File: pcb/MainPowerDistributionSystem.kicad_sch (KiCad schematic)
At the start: 6 parts, among them J2 PREC040DBAN-M71RC, U1 TPS22810DRV, U2 D24V7F5, U3 D24V7F3

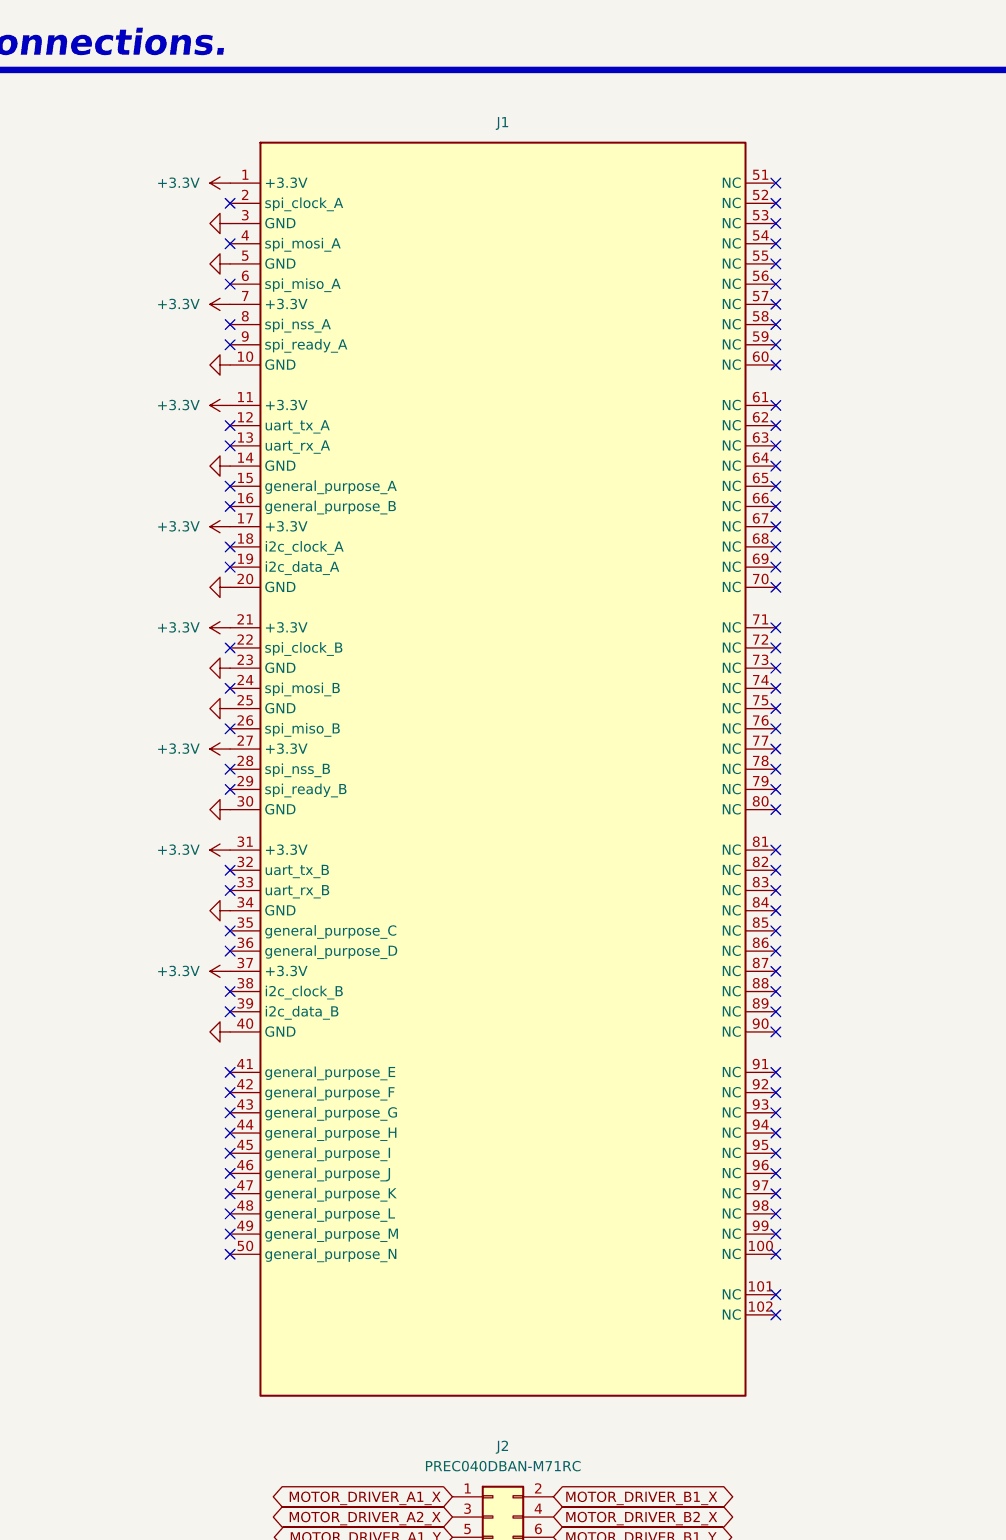
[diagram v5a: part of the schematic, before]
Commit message: Updated main stack-up connector design to go from 6 1x17 headers to only 4 1x17 headers.
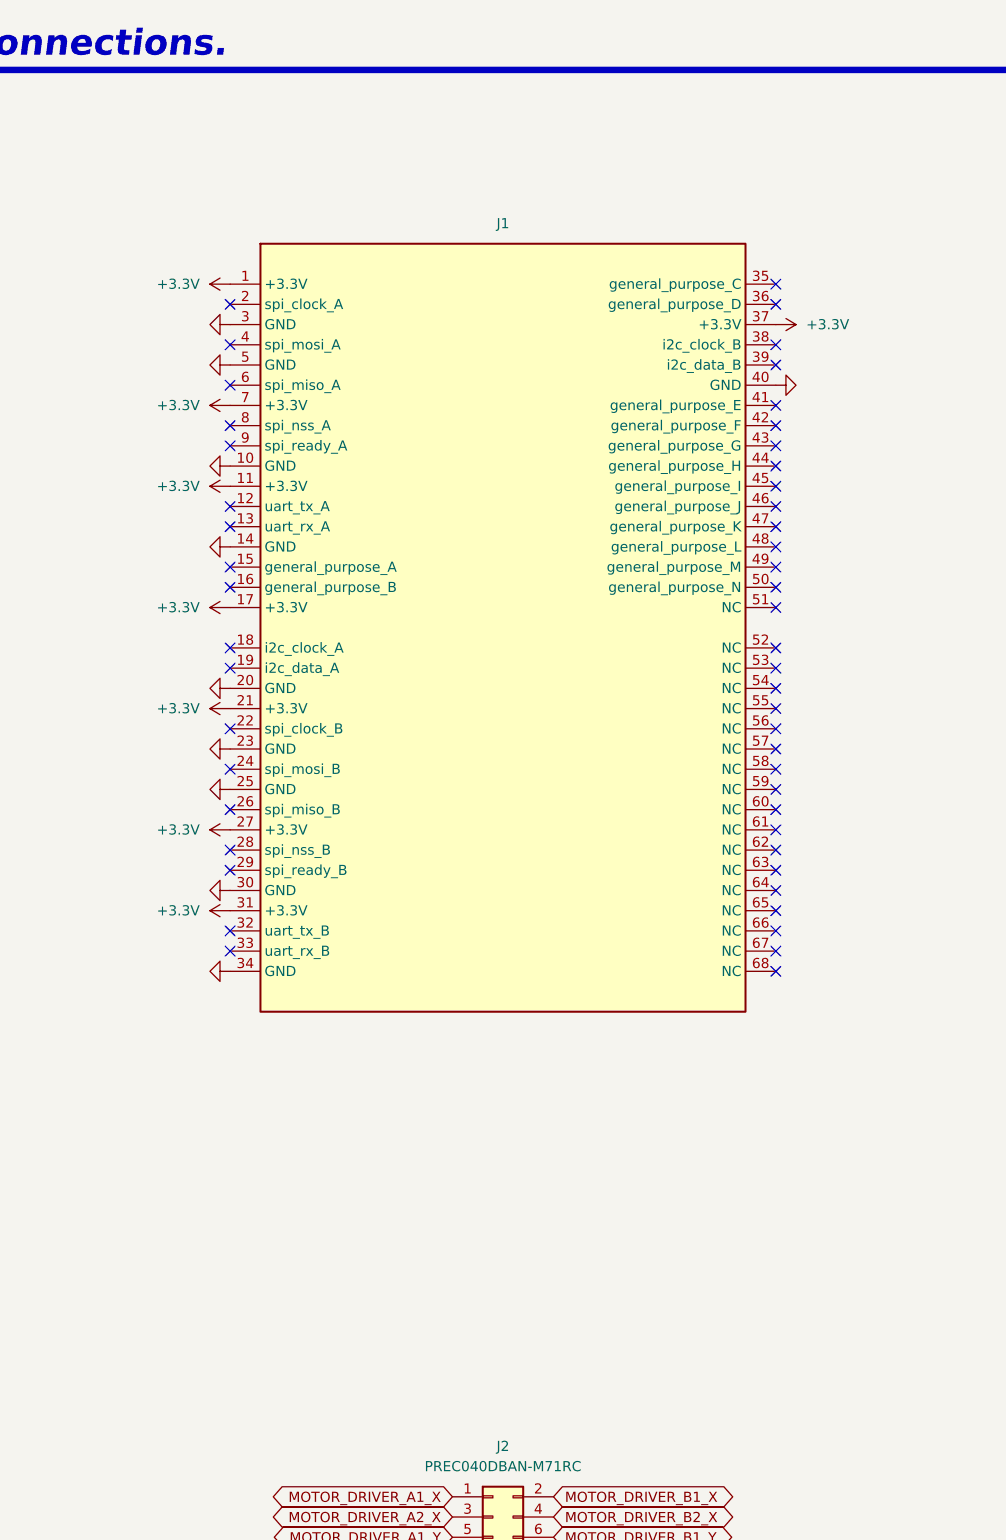
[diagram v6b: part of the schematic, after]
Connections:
- no-connect marks 86 -> 52

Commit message: Cleaned up and prepared `MainPowerDistributionSystem`.
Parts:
- removed R1: 1k, Resistor_SMD:R_1206_3216Metric_Pad1.30x1.75mm_HandSolder, symbol Device:R
- removed U1: TPS22810DRV, Package_SON:WSON-6-1EP_2x2mm_P0.65mm_EP1x1.6mm, symbol Power_Management:TPS22810DRV
- added C2, C3, C4, C5: 1u, Capacitor_SMD:C_1206_3216Metric_Pad1.33x1.80mm_HandSolder, symbol Device:C
- added R1, R3, R4, R5, R6, R7: 0, Resistor_SMD:R_1206_3216Metric_Pad1.30x1.75mm_HandSolder, symbol Device:R_Small
- added U1: D24V7F3, pcb:D24V7Fx, symbol D24V7Fx:D24V7Fx
- added U4, U8: BTS462TATMA1, Package_TO_SOT_SMD:TO-252-4, symbol Power_Management:BTS462TATMA1
- J2: footprint Connector_PinHeader_2.54mm:PinHeader_2x16_P2.54mm_Horizontal -> pcb:PinHeader_2x16_P2.54mm_Horizontal_SmallSilkscreen
- U2: value D24V7F5 -> D24V7F3
- U3: now not fitted
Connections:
- net +GSE-2 is gone; now on net +3.3V: J2.17 (Pin_17)
- net +TE-2 is gone; now on net +3.3V: J2.25 (Pin_25)
- net MOTOR_DRIVER_A1_X is gone; now on net +GSE-1: J2.1 (Pin_1)
- net MOTOR_DRIVER_A1_Y is gone; now on net +TE-1: J2.5 (Pin_5)
- net MOTOR_DRIVER_A2_X is gone; now on net GND: J2.3 (Pin_3)
- net MOTOR_DRIVER_A2_Y is gone; now on net GND: J2.7 (Pin_7)
- net MOTOR_DRIVER_A2_Z is gone; now on net GND: J2.11 (Pin_11)
- net MOTOR_DRIVER_B1_X is gone; now on net BURNWIRE_VOLTAGE: J2.2 (Pin_2)
- net MOTOR_DRIVER_B1_Y is gone; now on net BURNWIRE_VOLTAGE: J2.6 (Pin_6)
- net MOTOR_DRIVER_B2_X is gone; now on net GND: J2.4 (Pin_4)
- net MOTOR_DRIVER_B2_Y is gone; now on net GND: J2.8 (Pin_8)
- net +3.3V: now also J2.13 (Pin_13), J2.21 (Pin_21), C2.1, C3.1, C4.1, C5.1, R5.2, R6.2, R7.2; no longer U3.VOUT
- net +GSE-1: now also R1.1, R3.1, R4.1; no longer J2.13 (Pin_13)
- net +TE-1: now also U4.3 (Vbb), U8.3 (Vbb); no longer J2.21 (Pin_21)
- net BURNWIRE_VOLTAGE: now also U4.5 (OUT), U8.5 (OUT); no longer J2.30 (Pin_30)
- net GND: now also C2.2, C3.2, C4.2, C5.2, U1.GND, U4.1 (GND), U8.1 (GND); no longer J2.16 (Pin_16), J2.20 (Pin_20), J2.24 (Pin_24), J2.28 (Pin_28), J2.31 (Pin_31), J2.32 (Pin_32)
- net LOGIC_GSE_1: now also J1.48 (general_purpose_L)
- net LOGIC_TIMER_EVENT_1: now also J1.49 (general_purpose_M)
- net LOGIC_TIMER_EVENT_X: now reaches J1.50 (general_purpose_N)
- net +5V: no longer names the net of U2.VOUT
- net +5V: now also R6.1
- net +BATT-1: no longer names the net of J2.22 (Pin_22)
- net +BATT-2: no longer names the net of J2.26 (Pin_26)
- net +PLUGGED_3.3V: no longer names the net of U3.VIN
- net +PLUGGED_3.3V: now also R4.2
- net +PLUGGED_5V: no longer names the net of U2.VIN
- net +PLUGGED_5V: now also R3.2
- net +TE-3: no longer names the net of J2.29 (Pin_29)
- net +TE-RA: no longer names the net of J2.14 (Pin_14)
- net +TE-RB: no longer names the net of J2.18 (Pin_18)
- net MOTOR_DRIVER_A1_Z renamed +TE-X
- net MOTOR_DRIVER_B1_Z: no longer names the net of J2.10 (Pin_10)
- net MOTOR_DRIVER_B2_Z: no longer names the net of J2.12 (Pin_12)
- new net: R5.1, U1.VOUT
- new net: U4.2 (IN), U8.2 (IN)
- new net: R1.2, U1.VIN
- new net: R7.1, U3.VOUT
- no-connect marks 52 -> 62
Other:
- sheet Timer Event Logic Conversion - GSE-2 renamed Timer Event Logic Conversion - TE-X
- removed sheet Burnwire Regulator - 1
- removed sheet Burnwire Regulator - 2
- removed sheet Timer Event Logic Conversion - TE-2
- removed sheet Timer Event Logic Conversion - TE-3
- removed sheet Timer Event Logic Conversion - TE-RA
- removed sheet Timer Event Logic Conversion - TE-RB
- note added: "TODO: Add LEDs for when the burn-wire is active."
- note added: "TODO: Circuit here to turn the burn-wire automatically off after certain amount of time when TE-1 is activated."
- note removed: "Active-low inhibit. @/pg 2/tbl 2/`L4978`."
- note removed: "Burn-Wire."
- note removed: "Connections."
- note removed: "Logic Conversion."
- note removed: "Regulation."
- note removed: "TODO: Hardware enable."
- note removed: "TODO: LEDs."
- note removed: "The L4978 can handle at least 2A (typically 3A). In case we need more power, having two L4978 in parallel will allow for at least 4-6A (although without current limit). We can look into a chip that can handle a higher current output later if need be."
- note removed: "We can probably omit the decoupling capacitors for the input voltage."
- moved on the sheet: J1, J2

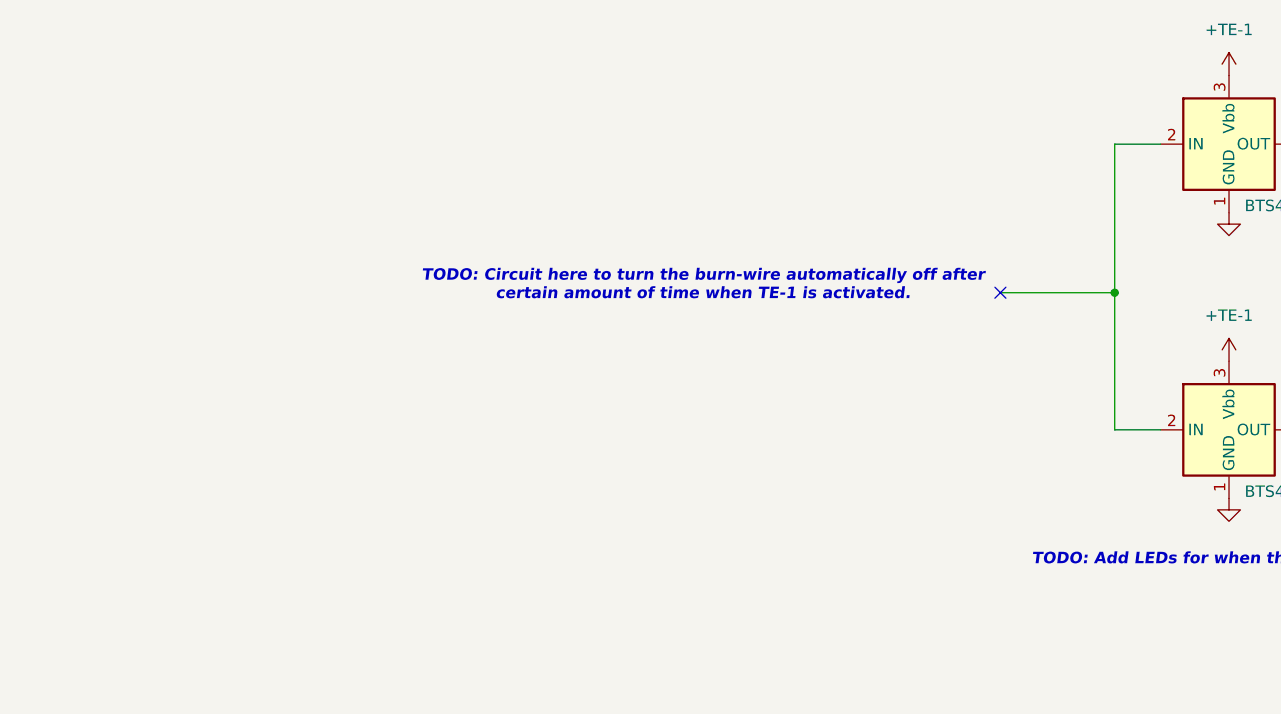
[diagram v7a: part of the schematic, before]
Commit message: Added burn wire timer to schematic and routed PCB
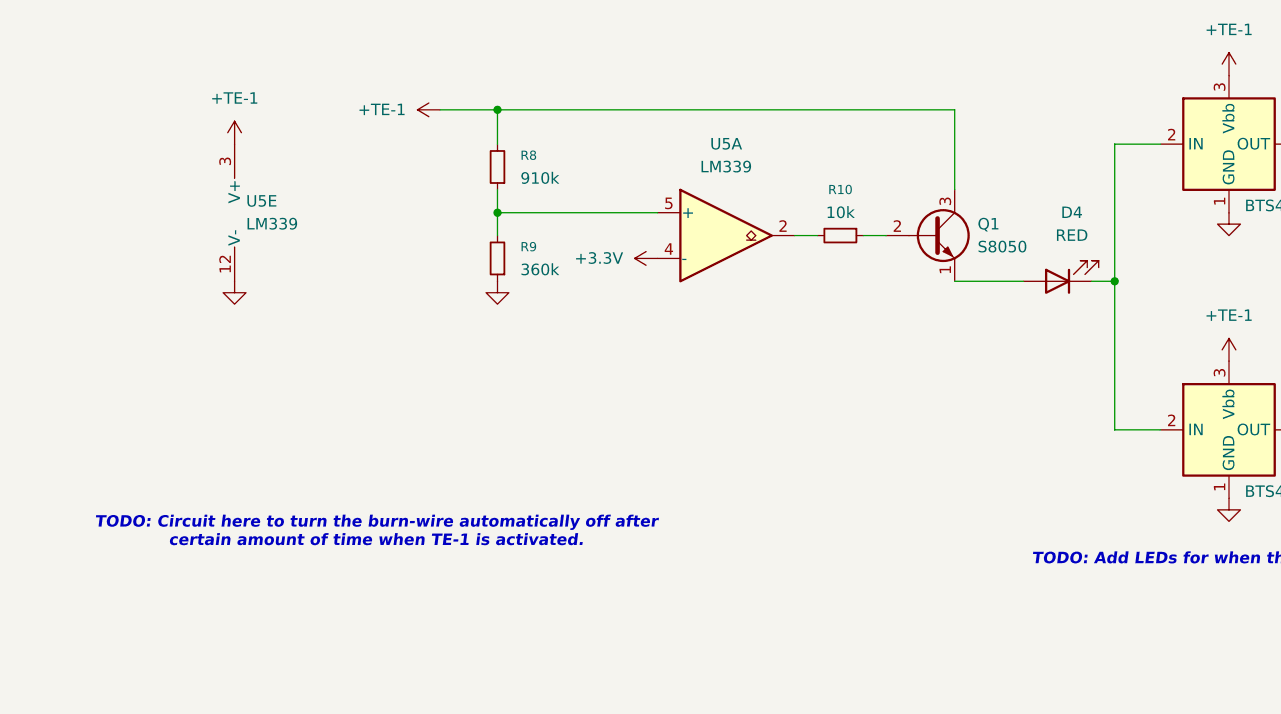
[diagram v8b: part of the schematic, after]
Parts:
- added D4: RED, LED_SMD:LED_1206_3216Metric_Pad1.42x1.75mm_HandSolder, symbol Device:LED
- added Q1: S8050, Package_TO_SOT_SMD:SOT-23_Handsoldering, symbol Transistor_BJT:S8050
- added R10: 10k, Resistor_SMD:R_1206_3216Metric_Pad1.30x1.75mm_HandSolder, symbol Device:R_Small
- added R8: 910k, Resistor_SMD:R_1206_3216Metric_Pad1.30x1.75mm_HandSolder, symbol Device:R_Small
- added R9: 360k, Resistor_SMD:R_1206_3216Metric_Pad1.30x1.75mm_HandSolder, symbol Device:R_Small
- added U5: LM339, symbol Comparator:LM339
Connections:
- net +3.3V: now also U5.4 (-)
- net +TE-1: now also Q1.3 (C), R8.2, U5.3 (V+)
- net GND: now also R9.1, U5.12 (V-)
- net at U4.2 (IN), U8.2 (IN): now also D4.1 (K)
- new net: R8.1, R9.2, U5.5 (+)
- new net: R10.2, U5.2
- new net: D4.2 (A), Q1.1 (E)
- new net: Q1.2 (B), R10.1
- no-connect marks 62 -> 61
